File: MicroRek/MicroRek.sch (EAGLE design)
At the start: 18 parts, among them IC3 LSM9DS1TR

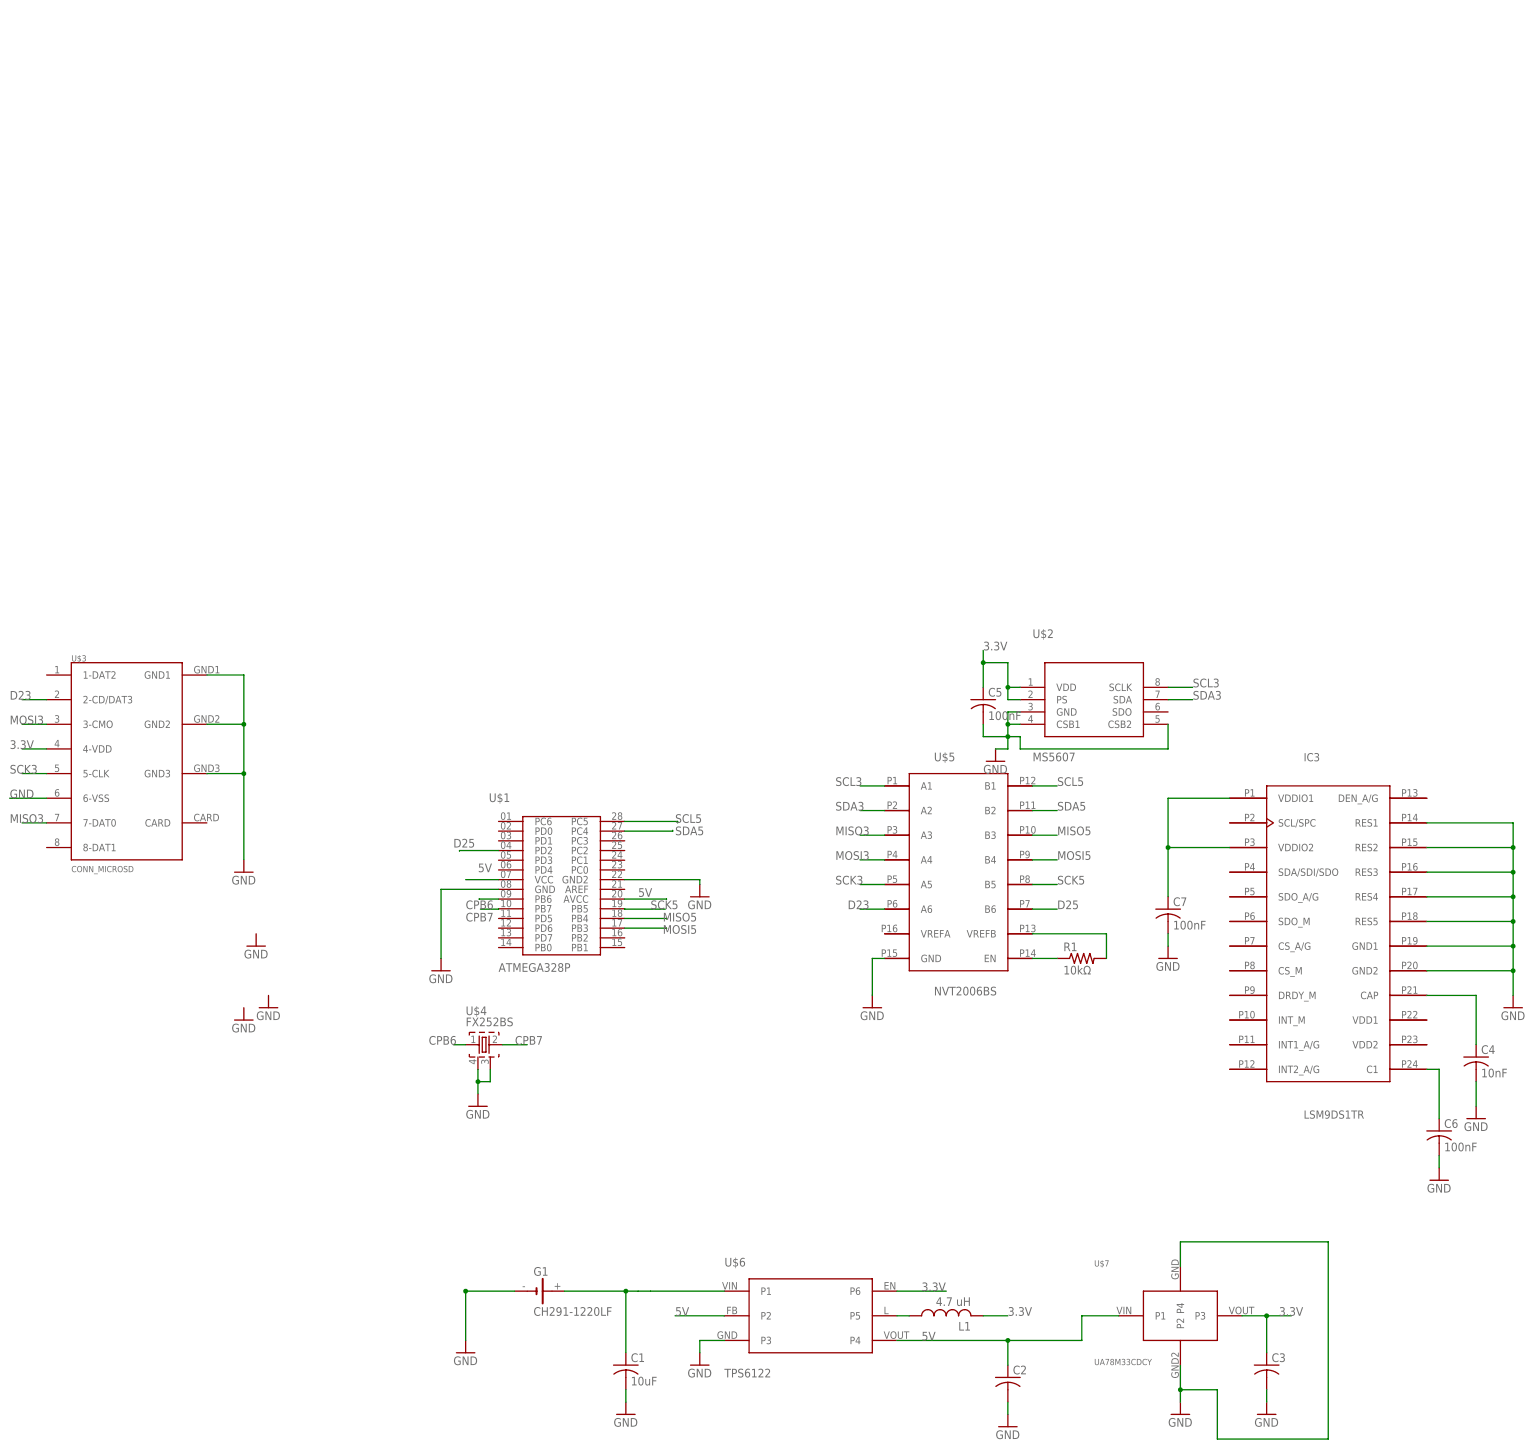
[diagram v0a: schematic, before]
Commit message: Added frame, replaced ATMEGA328P part
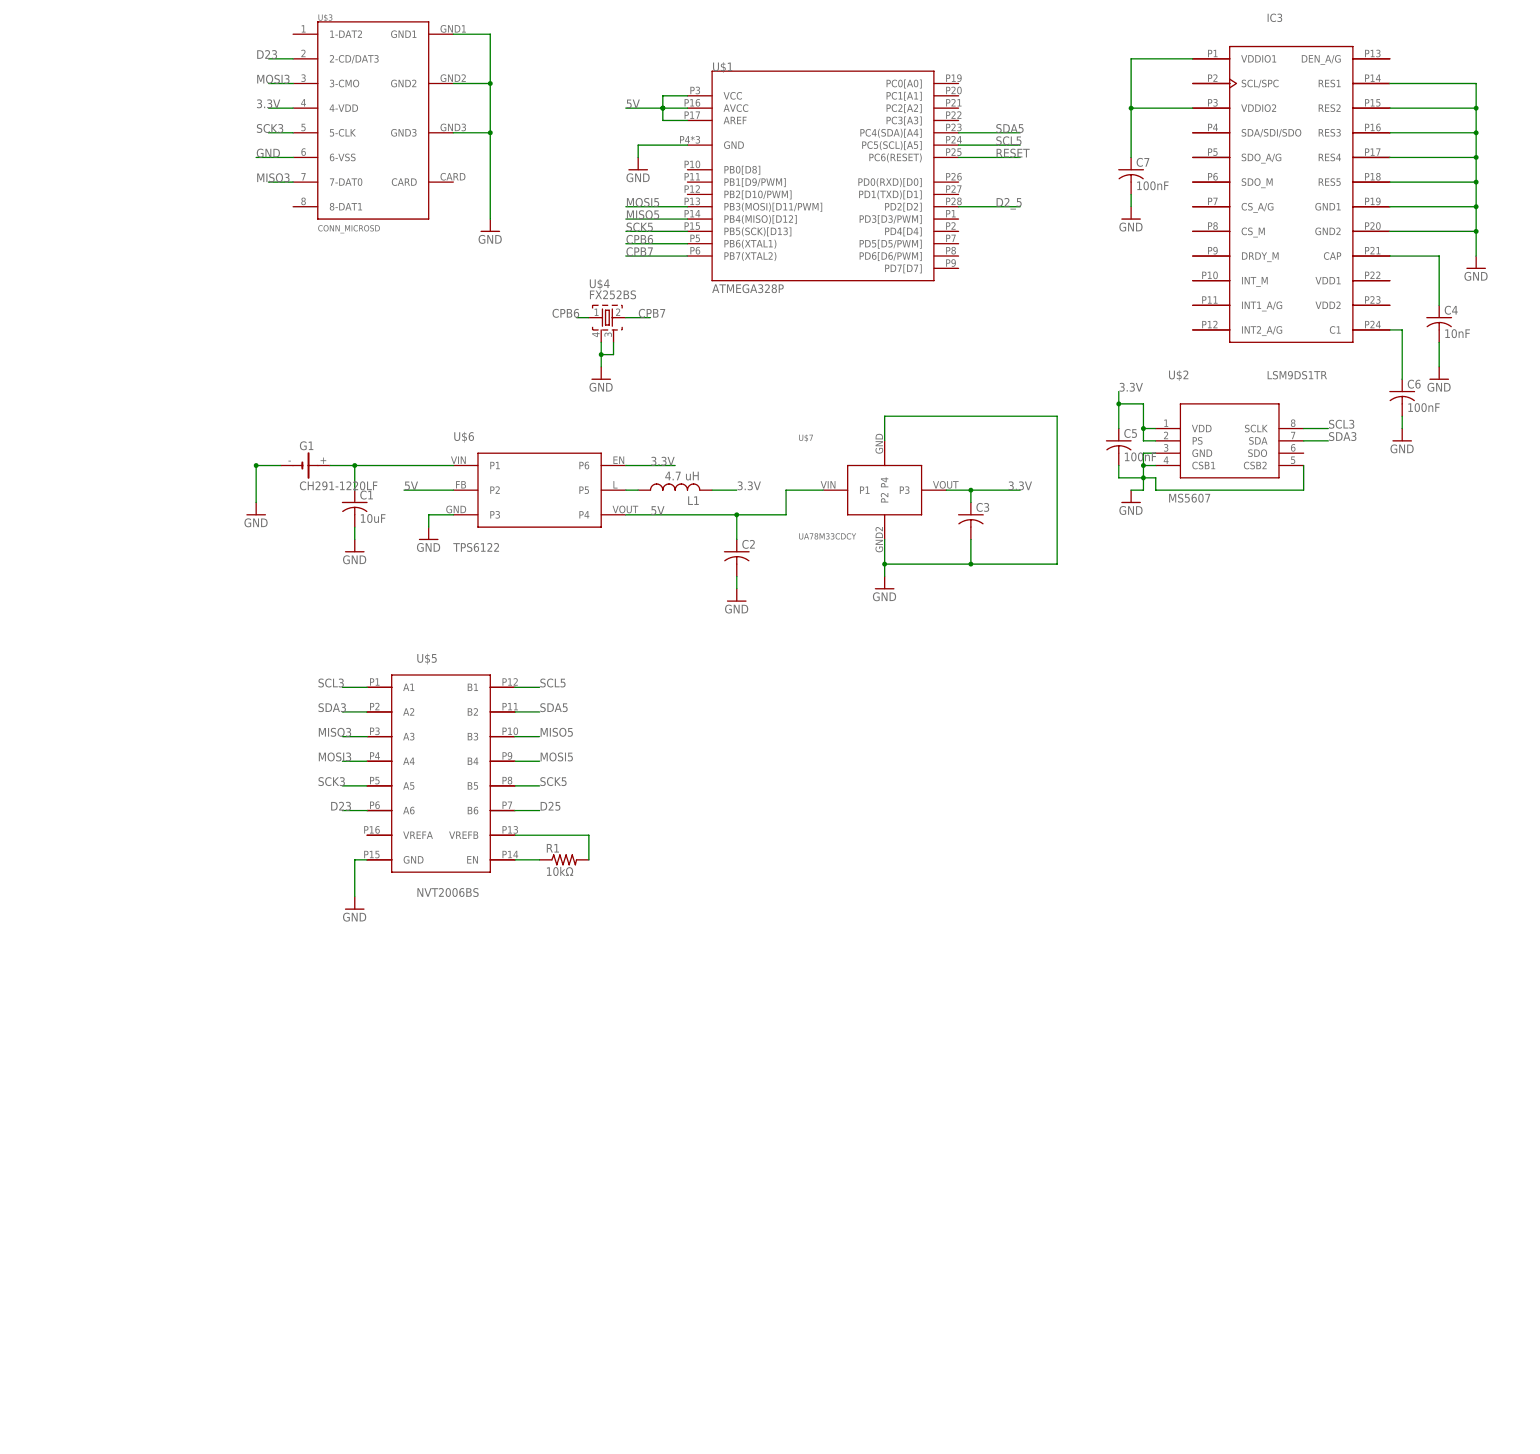
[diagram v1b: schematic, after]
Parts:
- U$1: device CPSS:ATMEGA328P -> CPSS_CPU:ATMEGA328P
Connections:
- new net D2_5: U$1.PD2[D2]
- new net RESET: U$1.PC6(RESET)
- net 5V: now also U$1.AREF
- net CPB6: now also U$1.PB6(XTAL1); no longer U$1.PB6
- net CPB7: now also U$1.PB7(XTAL2); no longer U$1.PB7
- net D25: no longer U$1.PD2
- net GND: no longer U$1.GND2
- net MISO5: now also U$1.PB4(MISO)[D12]; no longer U$1.PB4
- net MOSI5: now also U$1.PB3(MOSI)[D11/PWM]; no longer U$1.PB3
- net N$7: now also C7.1
- net SCK5: now also U$1.PB5(SCK)[D13]; no longer U$1.PB5
- net SCL5: now also U$1.PC5(SCL)[A5]; no longer U$1.PC5
- net SDA5: now also U$1.PC4(SDA)[A4]; no longer U$1.PC4
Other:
- moved on the sheet: C1, C2, C3, C4, C5, C6, C7, G1, IC3, L1, R1, U$2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
